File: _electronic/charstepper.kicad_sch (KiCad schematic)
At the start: 8 parts

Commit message: BETA first upload
nothing major done here:
* updated KiCAD files to v9
* removed alternative 6v feed-in. The proposed buck converter is fine.
* added to all components LCSC component IDs. With this, exporting the project as gerber files also automatically creates correct BOM for JLCPCB manufacturing
*
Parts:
- C_NEMA1: LCSC (none) -> C4747964
- C_NEMA2: LCSC (none) -> C96446
- D_NEMA1, D_NEMA2: LCSC (none) -> C2290
- J_NEMA1: LCSC (none) -> C32713263
- R_NEMA1, R_NEMA2: LCSC (none) -> C22775
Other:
- title: E-TKT v1.0 -> E-TKT v2.0 BETA

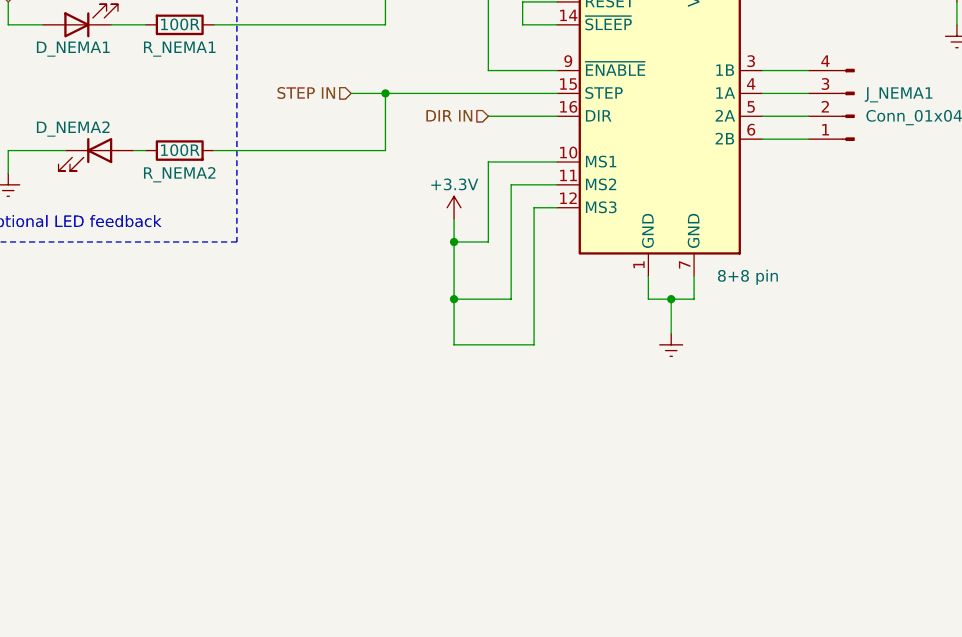
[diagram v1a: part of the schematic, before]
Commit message: Updated A_bottom in FreeCAD
added pockets for M3 nuts, added pockets for electronics cover

started to optimize pcb footprint layout and voltage reference planes
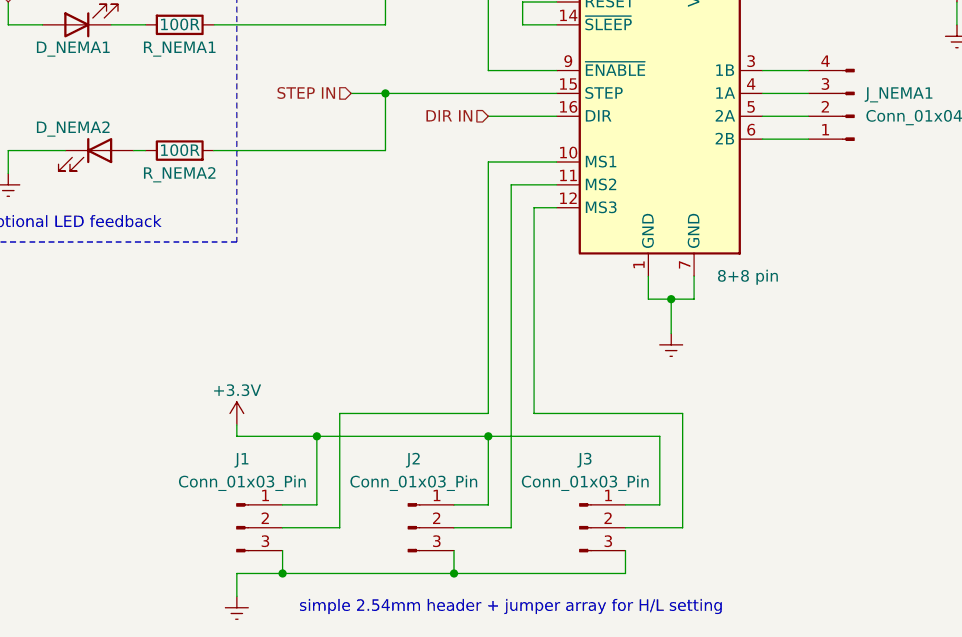
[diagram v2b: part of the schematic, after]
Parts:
- added J1, J2, J3: Conn_01x03_Pin, Connector_PinHeader_2.54mm:PinHeader_1x03_P2.54mm_Vertical, symbol Connector:Conn_01x03_Pin
- J_NEMA1: footprint Connector_PinHeader_2.54mm:PinHeader_1x04_P2.54mm_Horizontal -> Connector_PinHeader_2.54mm:PinHeader_1x04_P2.54mm_Vertical
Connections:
- net +3.3V: now also J1.1 (Pin_1), J2.1 (Pin_1), J3.1 (Pin_1); no longer A_NEMA1.10 (MS1), A_NEMA1.11 (MS2), A_NEMA1.12 (MS3)
- net GNDREF: now also J1.3 (Pin_3), J2.3 (Pin_3), J3.3 (Pin_3)
- new net: A_NEMA1.11 (MS2), J2.2 (Pin_2)
- new net: A_NEMA1.12 (MS3), J3.2 (Pin_2)
- new net: A_NEMA1.10 (MS1), J1.2 (Pin_2)
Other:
- note added: "simple 2.54mm header + jumper array for H/L setting"

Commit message: JLC export added, LCSC numbers updated
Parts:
- J1, J2, J3: LCSC (none) -> C2937625
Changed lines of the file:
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@@
+			)
+		)
+		(property "LCSC" "C2937625"
+			(at 121.92 152.4 0)
+			(effects
+				(font
+					(size 1.27 1.27)
+				)
+				(hide yes)
 			)
 		)
@@
 			)
 		)
+		(property "LCSC" "C2937625"
+			(at 140.97 152.4 0)
+			(effects
+				(font
+					(size 1.27 1.27)
+				)
+				(hide yes)
+			)
+		)
 		(pin "2"
 		)
@@
 			(at 102.87 152.4 0)
 			(effects
+				(font
+					(size 1.27 1.27)
+				)
+				(hide yes)
+			)
+		)
+		(property "LCSC" "C2937625"
+			(at 102.87 152.4 0)
+			(effects

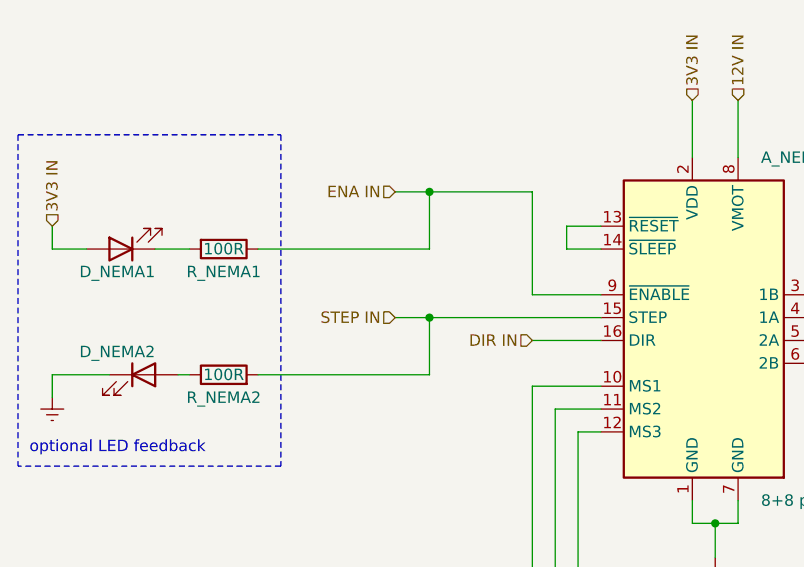
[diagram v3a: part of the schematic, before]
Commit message: Updated layout of schematic symbol's text
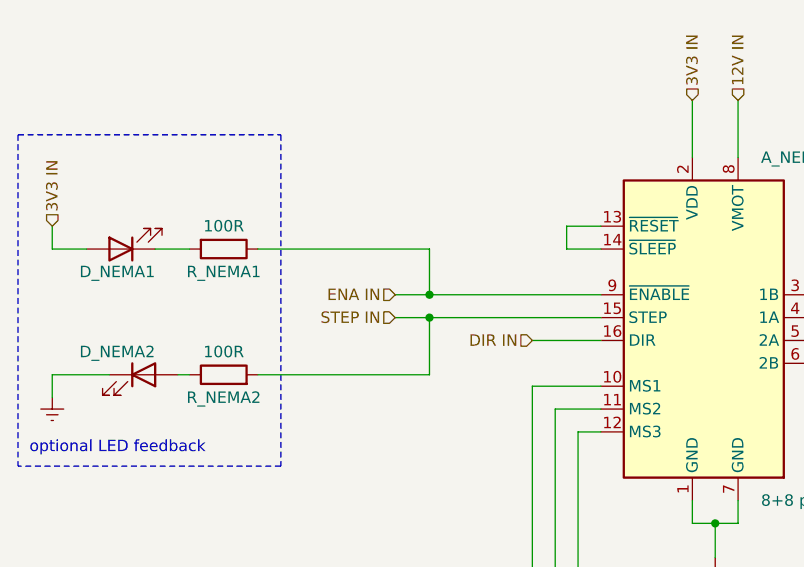
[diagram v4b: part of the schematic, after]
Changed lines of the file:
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@@
+	)
+	(junction
+		(at 119.38 101.6)
+		(diameter 0)
+		(color 0 0 0 0)
 	)
 	(junction
@@
 		(color 0 0 0 0)
 	)
-	(junction
-		(at 119.38 90.17)
-		(diameter 0)
-		(color 0 0 0 0)
-	)
 	(wire
 		(pts
@@
 	(wire
 		(pts
-			(xy 115.57 90.17) (xy 119.38 90.17)
-		)
-		(stroke
-			(width 0)
-			(type default)
-		)
-	)
-	(wire
-		(pts
-			(xy 119.38 90.17) (xy 119.38 96.52)
+			(xy 115.57 101.6) (xy 119.38 101.6)
+		)
+		(stroke
+			(width 0)
+			(type default)
+		)
+	)
+	(wire
+		(pts
+			(xy 119.38 101.6) (xy 119.38 96.52)
 		)
 		(stroke
@@
 	(wire
 		(pts
-			(xy 130.81 101.6) (xy 138.43 101.6)
-		)
-		(stroke
-			(width 0)
-			(type default)
-		)
-	)
-	(wire
-		(pts
 			(xy 133.35 114.3) (xy 138.43 114.3)
 		)
@@
 	(wire
 		(pts
-			(xy 130.81 90.17) (xy 130.81 101.6)
-		)
-		(stroke
-			(width 0)
-			(type default)
-		)
-	)
-	(wire
-		(pts
 			(xy 138.43 93.98) (xy 134.62 93.98)
 		)
@@
 	(wire
 		(pts
-			(xy 119.38 90.17) (xy 130.81 90.17)
+			(xy 119.38 101.6) (xy 138.43 101.6)
 		)
 		(stroke
@@
 	(hierarchical_label "ENA IN"
 		(shape input)
-		(at 115.57 90.17 180)
+		(at 115.57 101.6 180)
 		(effects
 			(font
@@
 		)
 		(property "Value" "100R"
-			(at 96.52 110.49 90)
+			(at 96.52 107.95 90)
 			(effects
 				(font
@@
 		)
 		(property "Value" "100R"
-			(at 96.52 96.52 90)
-			(effects
-				(font
+			(at 96.52 93.98 90)
+			(effects
+				(font
